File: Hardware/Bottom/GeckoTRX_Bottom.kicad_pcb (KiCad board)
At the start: 4 copper layers, 120 x 80 mm, 177 parts, among them J1 Jack-DC, J10 Conn_01x04_Female, J11 Conn_01x04_Female, J12 Conn_01x03_Female, J13 Conn_01x03_Female, J14 Conn_01x03_Female, J15 Conn_01x03_Female, J16 Conn_01x03_Female, J17 Conn_01x03_Female, J18 Conn_01x03_Female, J19 Conn_01x03_Female, J2 Conn_Coaxial, J20 Conn_01x03_Female, J21 Conn_01x03_Female, J22 Conn_01x03_Female, J23 Conn_01x03_Female, J24 Conn_01x03_Female, J25 Conn_01x03_Female, J26 Conn_01x03_Female, J27 Conn_01x03_Female, J28 Conn_01x03_Female, J29 Conn_01x03_Female, J3 Conn_02x05_Odd_Even, J30 Conn_01x03_Female, J31 Conn_01x03_Female, J32 Conn_01x03_Female, J4 Conn_02x05_Odd_Even, J5 Conn_01x04_Female, J6 Conn_01x04_Female, J7 Conn_01x04_Female, J8 Conn_01x04_Female, J9 Conn_01x04_Female, K4 G6K-2, T1 MABA-007237-ETC410, U1 TPS562200, U10 74LVC1G17, U11 74HC74D, U2 SN74CBTLV3253, U3 LT6231, U4 OP491-4, U5 MCP23017_ML, U6 Si5351A-B-GM, U7 MCP23017_ML, Y1 25MHz

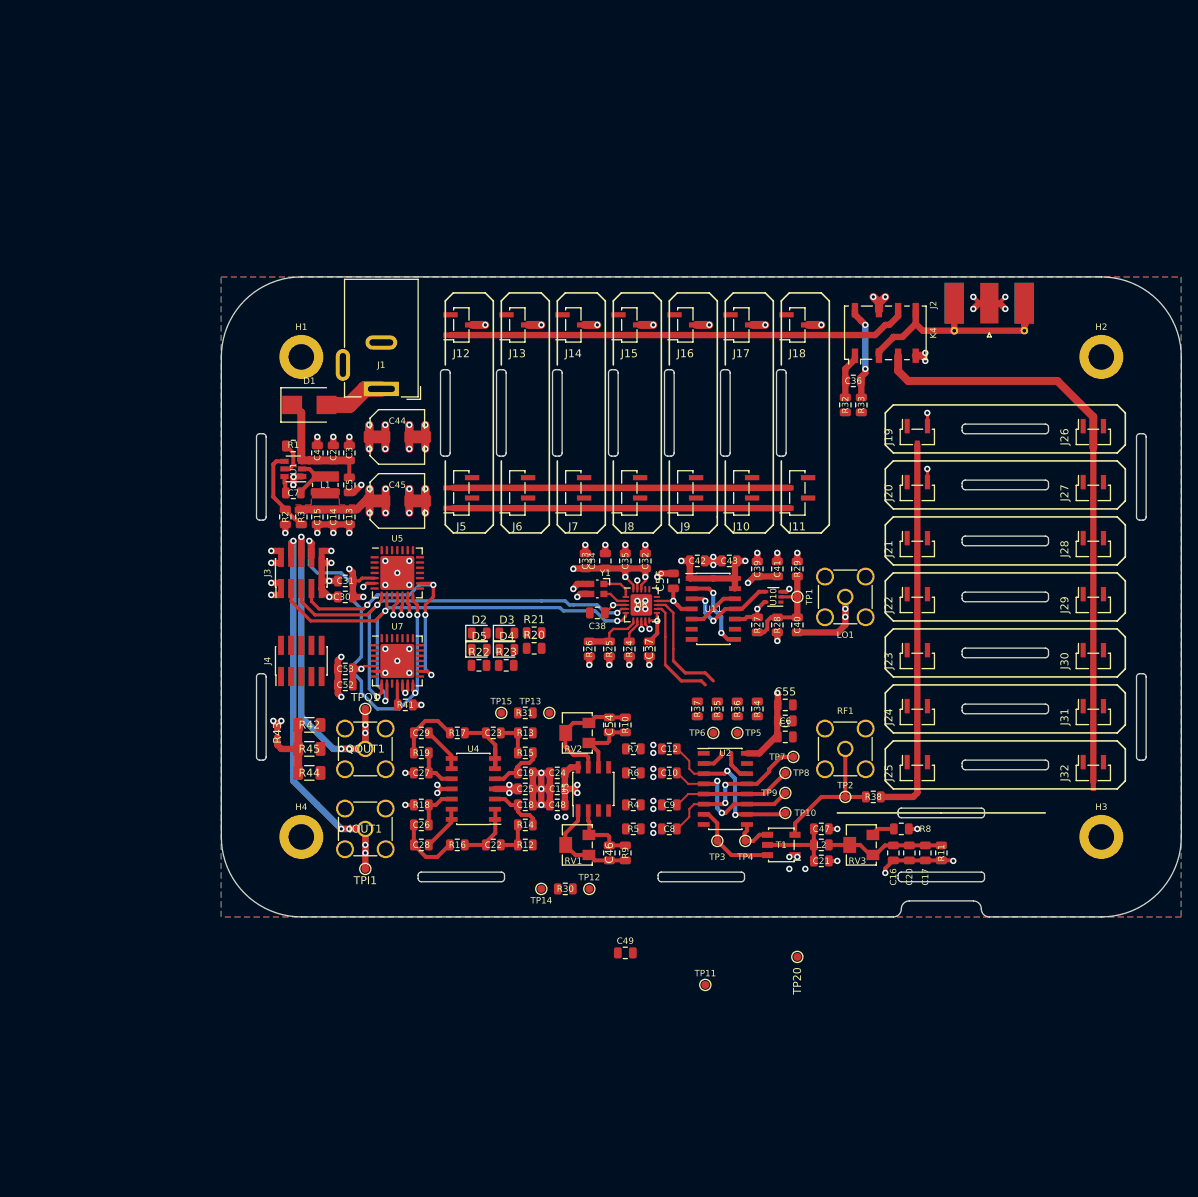
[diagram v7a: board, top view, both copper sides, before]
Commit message: PCB v2 0 airwires
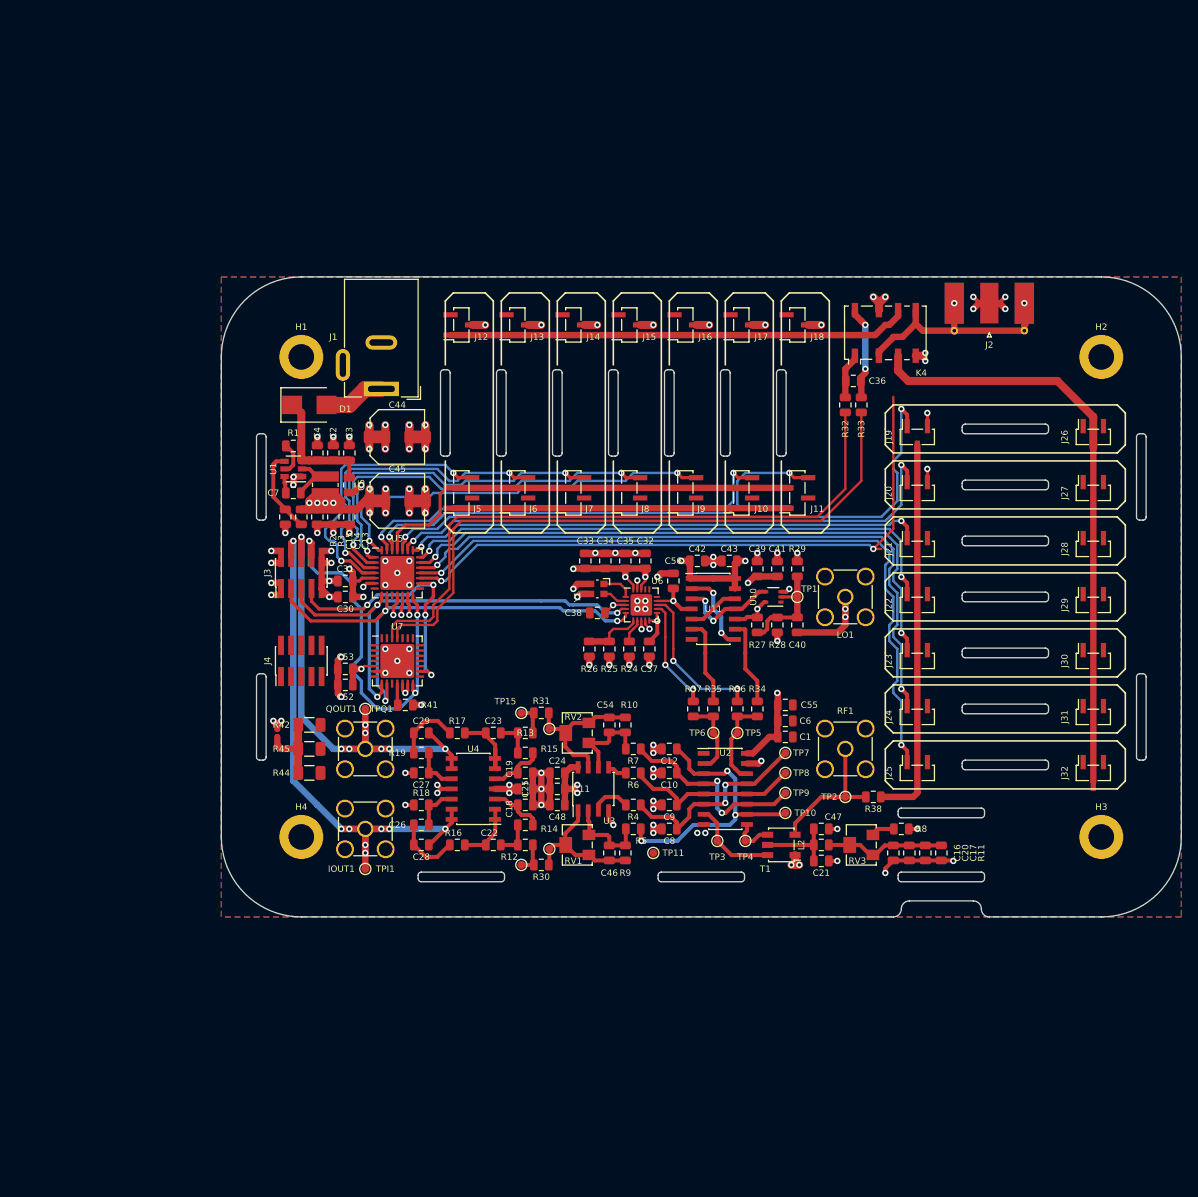
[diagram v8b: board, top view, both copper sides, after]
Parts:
- removed C49: 100n, Capacitor_SMD:C_0805_2012Metric
- removed D2, D3, D4, D5: LED, LED_SMD:LED_0805_2012Metric
- removed R20, R21, R22, R23: 100, Resistor_SMD:R_0805_2012Metric
- removed TP20: 1V65, TestPoint:TestPoint_Pad_D1.0mm
- moved TP11 17.7 mm to (-6.00, 32.0)
- moved TP12 7.07 mm to (-19.0, 31.5)
- moved R30 4.24 mm to (-20.0, 33.5)
- moved TP14 3.91 mm to (-22.5, 33.5)
- moved TP15 2.50 mm to (-22.5, 14.5)
- moved R31 2.00 mm to (-20.0, 14.5)
- moved TP13 2.00 mm to (-19.0, 16.5)
- moved TP7 1.12 mm to (10.5, 19.5)
- moved R35 0.50 mm to (1.50, 14.0)
- moved R37 0.50 mm to (-1.00, 14.0)
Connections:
- net Net-(U5-Pad17) renamed /Filter/EN_PRE_TEST
- R32 pad 1: /GPIO Expander/GPIO_0 -> /GPIO Expander/GPIO_1
- R33 pad 1: /GPIO Expander/GPIO_1 -> /GPIO Expander/GPIO_0
- U5 pad 1: Net-(U5-Pad1) -> /Filter/SW_LP_20
- U5 pad 18: Net-(U5-Pad18) -> /Filter/EN_PRE_CUS
- U5 pad 19: Net-(U5-Pad19) -> /Filter/EN_PRE_10
- U5 pad 2: Net-(U5-Pad2) -> /Filter/SW_LP_40
- U5 pad 20: Net-(U5-Pad20) -> /Filter/EN_PRE_15
- U5 pad 21: Net-(U5-Pad21) -> /Filter/EN_PRE_20
- U5 pad 22: Net-(U5-Pad22) -> /Filter/EN_PRE_40
- U5 pad 23: Net-(U5-Pad23) -> /Filter/EN_PRE_80
- U5 pad 24: Net-(U5-Pad24) -> /Filter/EN_PRE_160
- U5 pad 25: Net-(U5-Pad25) -> /Filter/REL_COM
- U5 pad 26: Net-(U5-Pad26) -> /Filter/SW_LP_CUST
- U5 pad 27: Net-(U5-Pad27) -> /Filter/SW_LP_10
- U5 pad 28: Net-(U5-Pad28) -> /Filter/SW_LP_15
- U5 pad 3: Net-(U5-Pad3) -> /Filter/SW_LP_80
- U5 pad 4: Net-(U5-Pad4) -> /Filter/SW_LP_160
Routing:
- net /Filter/EN_PRE_CUS: track 0.00 -> 89.3 mm, vias 0 -> 2
- net /Filter/EN_PRE_10: track 0.00 -> 82.9 mm, vias 0 -> 2
- net /GPIO Expander/GPIO_0: track 0.00 -> 80.9 mm
- net /GPIO Expander/GPIO_1: track 0.00 -> 80.3 mm
- net /Filter/EN_PRE_TEST: track 0.00 -> 80.2 mm, vias 0 -> 2
- net /Filter/EN_PRE_160: track 0.00 -> 79.7 mm, vias 0 -> 2
- net /Filter/EN_PRE_15: track 0.00 -> 76.6 mm, vias 0 -> 2
- net /Filter/EN_PRE_80: track 0.00 -> 71.9 mm, vias 0 -> 2
- net /Filter/EN_PRE_20: track 0.00 -> 69.6 mm, vias 0 -> 2
- net /Filter/EN_PRE_40: track 0.00 -> 65.3 mm, vias 0 -> 2
- net /Filter/SW_LP_CUST: track 0.00 -> 59.8 mm, vias 0 -> 2
- net /Filter/SW_LP_10: track 0.00 -> 54.2 mm, vias 0 -> 2
- net /Filter/SW_LP_15: track 0.00 -> 50.7 mm, vias 0 -> 2
- net /Filter/SW_LP_20: track 0.00 -> 49.3 mm, vias 0 -> 2
- net /Filter/SW_LP_40: track 0.00 -> 44.0 mm, vias 0 -> 2
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- removed copper zone on F.Cu, net +3V3
